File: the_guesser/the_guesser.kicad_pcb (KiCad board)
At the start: 4 copper layers, 24 x 72 mm, 59 parts, among them J1 USB_B_Mini, J2 Conn_Coaxial, J3 RFShield_TwoPieces, U2 ESP32-S3, U3 W25Q128JVS, U5 CC1101RGPR, U6 CC1190RGVR, U7 B39921B3728U410, X1 STDCRG2-27M, X2 ECS-3953M-400-AU-TR

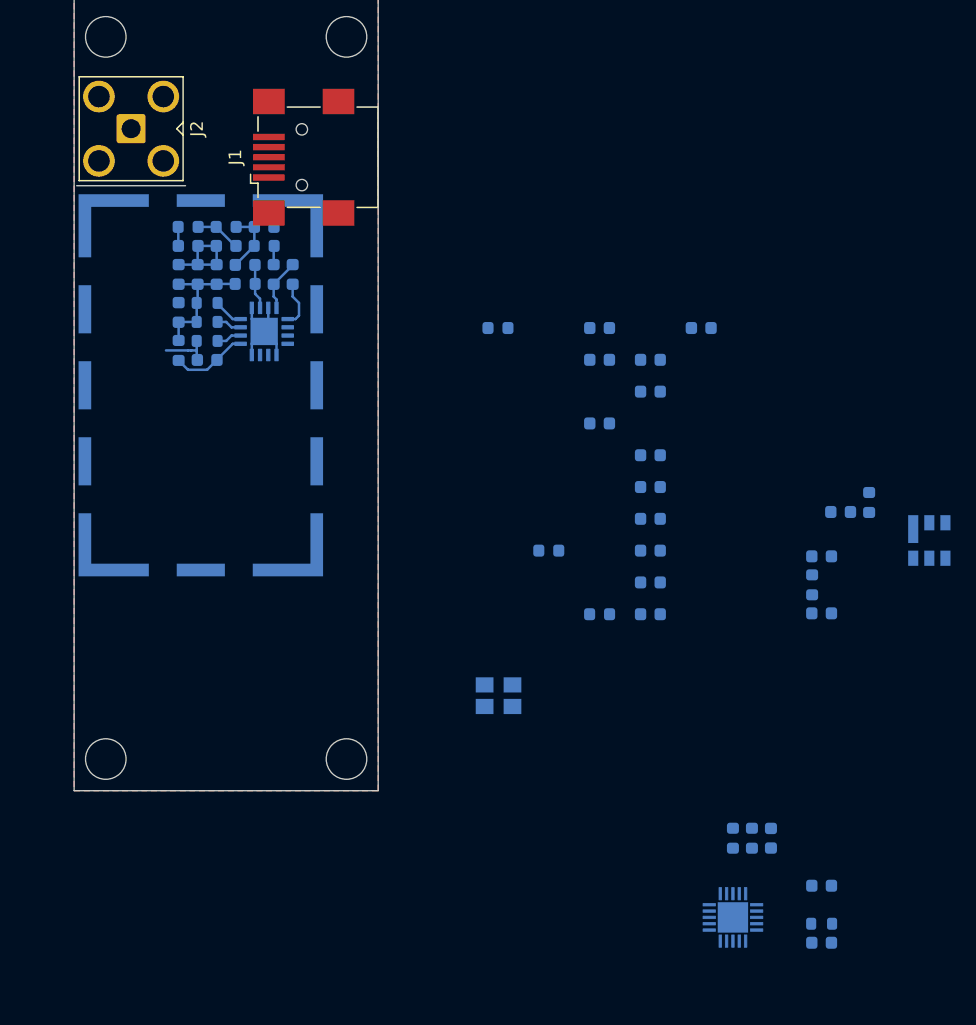
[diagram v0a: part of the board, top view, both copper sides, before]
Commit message: Routed Guesser RF components
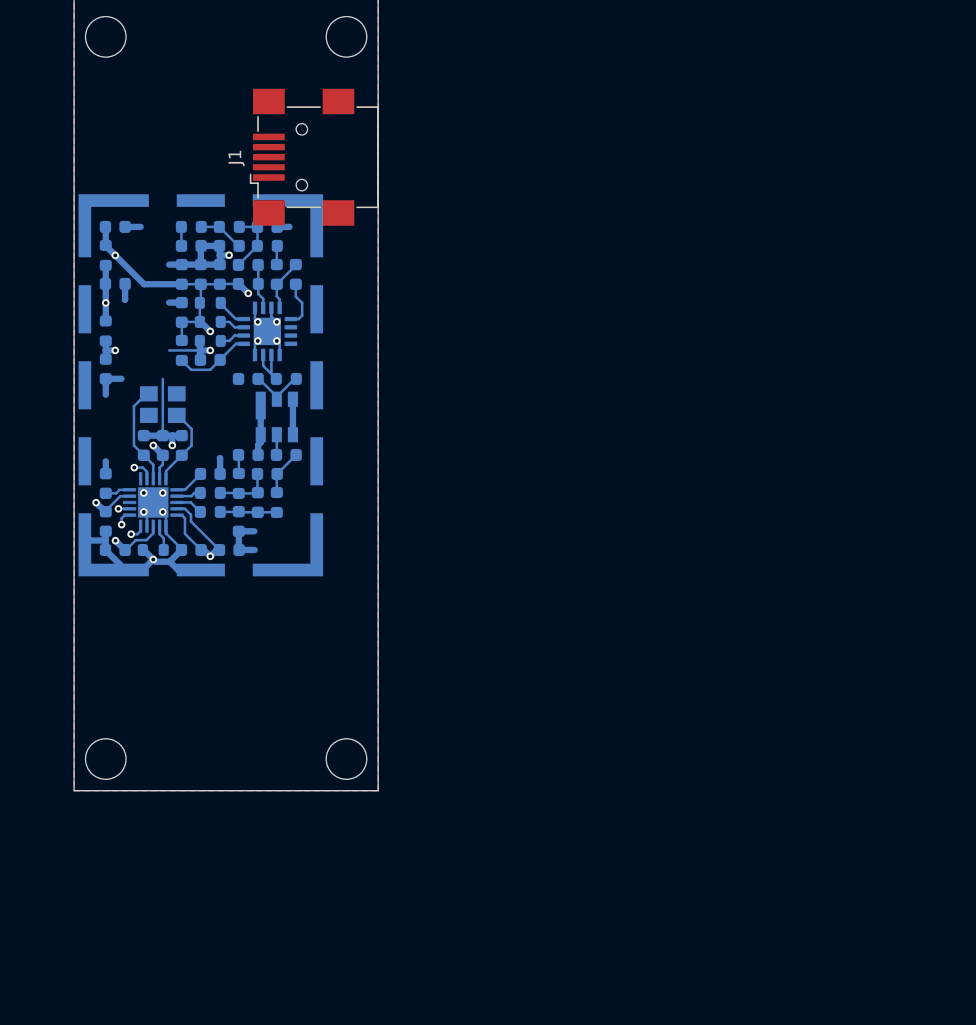
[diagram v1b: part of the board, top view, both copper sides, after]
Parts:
- removed J2: Conn_Coaxial, Connector_Coaxial:SMA_Amphenol_901-143_Horizontal
- J3: value RFShield_TwoPieces -> BMI-S-209-F
- moved C181 63.8 mm to (203.2, 81.0), turned to 0 degrees
- moved C2 61.5 mm to (203.2, 55.5)
- moved C3 61.5 mm to (203.2, 60.0)
- moved L2 61.5 mm to (202.5, 57.8)
- moved R171 60.4 mm to (206.2, 81.0), turned to 0 degrees
- moved C151 56.4 mm to (209.2, 81.0), turned to 0 degrees
- moved U5 56.3 mm to (206.2, 77.2), turned to 0 degrees
- moved U7 52.4 mm to (216.0, 70.5)
- moved L131 49.9 mm to (210.8, 78.0), turned to 180 degrees
- moved L121 49.4 mm to (210.8, 76.5), turned to 0 degrees
- moved C141 48.4 mm to (212.2, 81.0), turned to 180 degrees
- moved C125 47.9 mm to (213.8, 67.5)
- moved C1 47.1 mm to (202.5, 66.7), turned to -90 degrees
- moved L25 47.0 mm to (216.8, 67.5), turned to 180 degrees
- moved L1 44.9 mm to (202.5, 63.7), turned to -90 degrees
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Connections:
- net Net-(U5-AVDD_11) renamed VCC_{CC1101}
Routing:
- net VCC_{CC1101}: track 0.00 -> 54.9 mm, vias 0 -> 5
- net GND: track 20.2 -> 62.5 mm, vias 0 -> 12
- net VCC_{CC1190}: track 10.4 -> 36.4 mm, vias 0 -> 3
- net XOSC_Q1: track 0.00 -> 7.74 mm
- net XOSC_Q2: track 0.00 -> 6.29 mm
- net Net-(C121-Pad2): track 0.00 -> 4.38 mm
- net VCC: track 0.00 -> 4.34 mm, vias 0 -> 1
- net Net-(C121-Pad1): track 0.00 -> 4.31 mm
- net Net-(U7-IN): track 0.00 -> 3.96 mm
- net LNA_OUT: track 0.00 -> 3.82 mm
- net Net-(C122-Pad1): track 0.00 -> 3.56 mm
- net RF_N: track 0.00 -> 2.15 mm
- net Net-(U5-RBIAS): track 0.00 -> 2.01 mm
- net Net-(U5-DCOUPL): track 0.00 -> 1.99 mm
- net RF_P: track 0.00 -> 1.95 mm
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
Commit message: Started Guesser sensor selection
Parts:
- removed X2: ECS-3953M-400-AU-TR, Crystal:Crystal_SMD_5032-4Pin_5.0x3.2mm
- added BT1: Battery_Cell, locals_but_working_PLEASE:CONN2_1775469-2_TEC, F.Cu at (212.0, 100.0)
- added C4: 10u, Capacitor_SMD:C_0603_1608Metric, B.Cu at (207.8, 98.8)
- added D1: MB6S, Package_TO_SOT_SMD:TO-269AA, B.Cu at (212.0, 95.5)
- added J4: Screw_Terminal_01x06, TerminalBlock_Phoenix:TerminalBlock_Phoenix_MPT-0,5-6-2.54_1x06_P2.54mm_Horizontal, F.Cu at (215.6, 42.4)
- added J5: Screw_Terminal_01x06, TerminalBlock_Phoenix:TerminalBlock_Phoenix_MPT-0,5-6-2.54_1x06_P2.54mm_Horizontal, F.Cu at (208.4, 29.6)
- added L3: 0.47u, Inductor_SMD:L_0603_1608Metric, B.Cu at (207.8, 91.5)
- added R2: 5.36k, Resistor_SMD:R_0603_1608Metric, B.Cu at (208.5, 96.5)
- added R3: 1.2k, Resistor_SMD:R_0603_1608Metric, B.Cu at (207.0, 96.5)
- added U10: TPS61033DRLR, Package_TO_SOT_SMD:SOT-583-8, B.Cu at (207.8, 93.7)
- added U8: MS5607-02BA, Package_LGA:LGA-8_3x5mm_P1.25mm, F.Cu at (228.9, 87.1)
- moved U3 85.2 mm to (235.5, 77.0)
- moved U2 78.5 mm to (212.0, 75.0), turned to -45 degrees
- moved J1 37.9 mm to (206.0, 86.0), turned to -90 degrees
- moved C1 8.98 mm to (204.5, 58.0)
- moved X1 8.98 mm to (209.0, 60.8)
- moved C101 8.98 mm to (210.5, 64.0)
- moved C111 8.98 mm to (212.8, 66.2)
- moved C121 8.98 mm to (216.5, 68.5)
- moved C122 8.98 mm to (217.2, 66.2)
- moved C123 8.98 mm to (218.8, 64.8)
- moved C124 8.98 mm to (215.8, 64.8)
- moved C125 8.98 mm to (215.8, 58.8)
- moved C131 8.98 mm to (215.0, 70.0)
- moved C132 8.98 mm to (212.8, 57.2)
- moved C141 8.98 mm to (214.2, 72.2)
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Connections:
- net V_{BAT} renamed V_{USB}
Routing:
- net VCC: track 4.34 -> 13.1 mm, vias 1 -> 3
- net /BT-: track 0.00 -> 6.19 mm, vias 0 -> 1
- net /BT+: track 0.00 -> 6.19 mm, vias 0 -> 1
- net V_{B}: track 0.00 -> 5.02 mm
- net Net-(U10-FB): track 0.00 -> 3.04 mm
- net Net-(U10-SW): track 0.00 -> 2.76 mm
- net GND: track 62.5 -> 63.5 mm

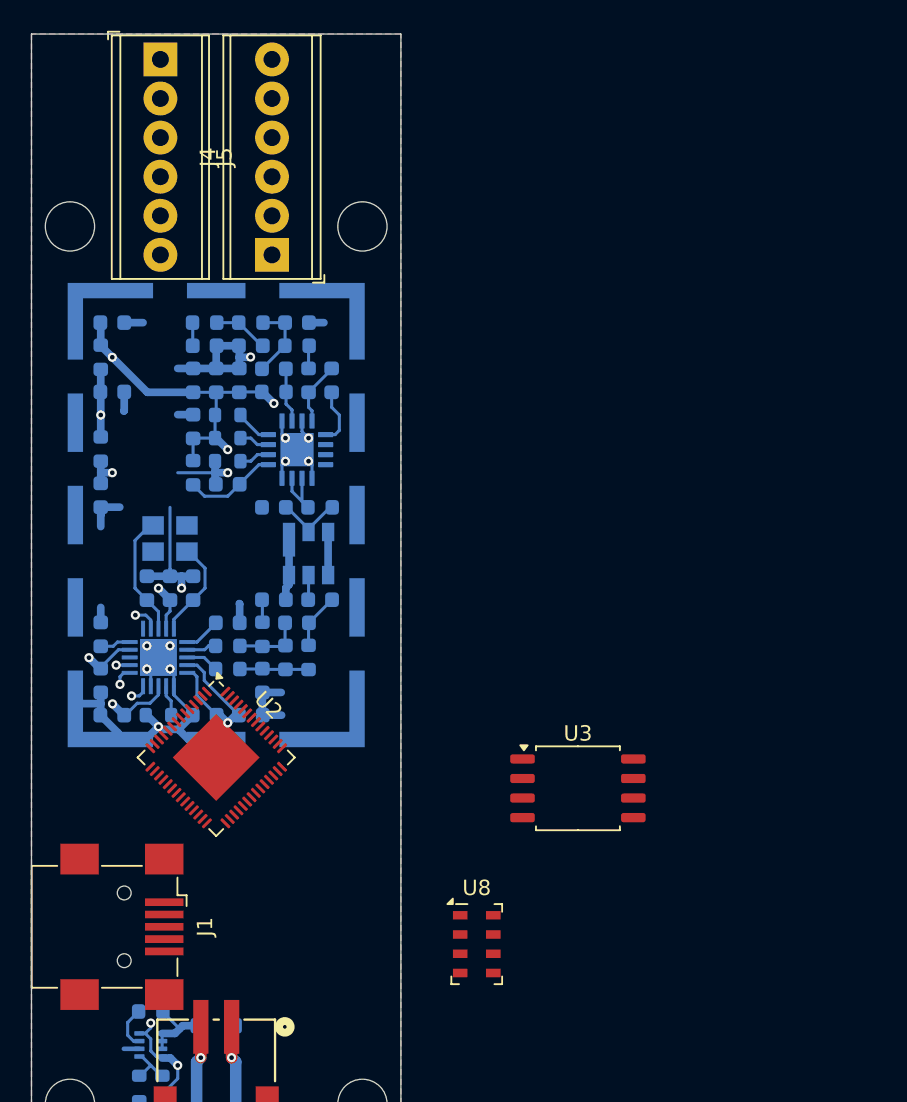
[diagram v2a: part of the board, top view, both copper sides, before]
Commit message: Started Guesser I/O and continued sensor selection
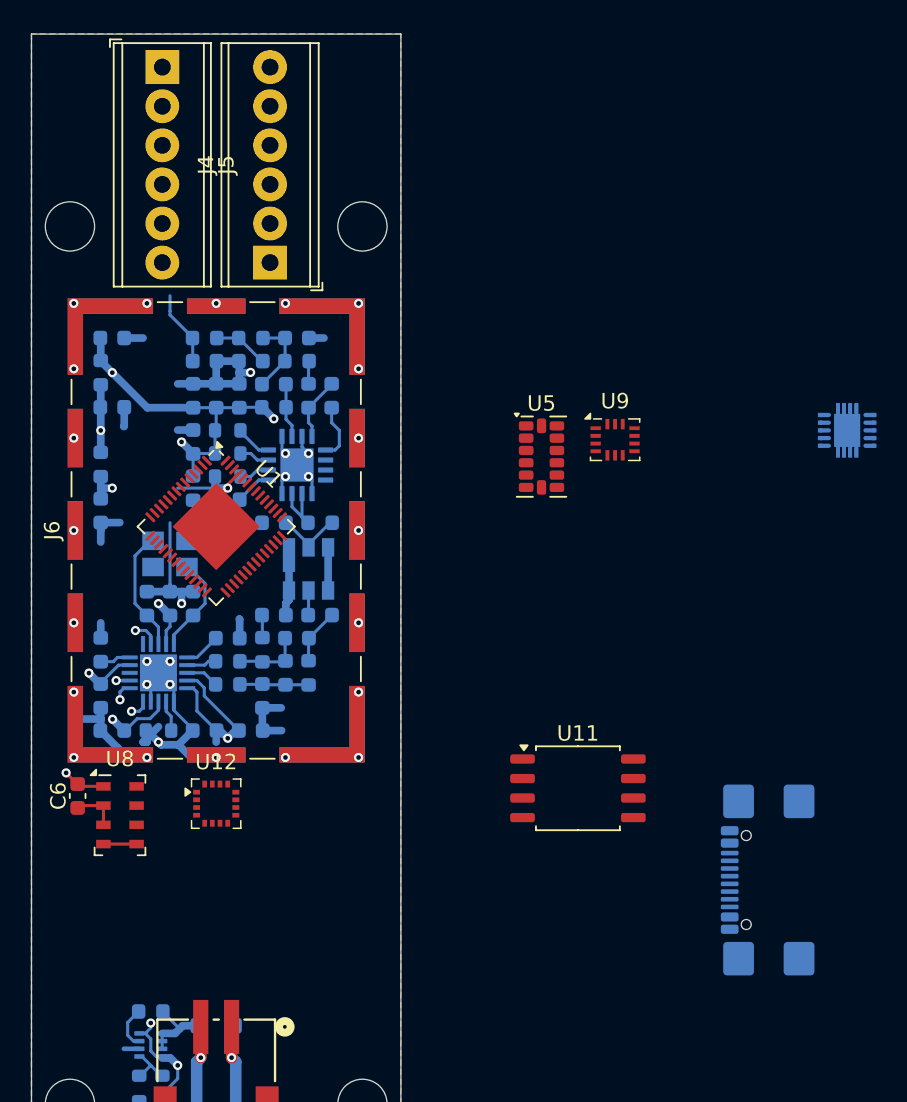
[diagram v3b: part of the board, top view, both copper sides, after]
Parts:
- removed J1: USB_B_Mini, Connector_USB:USB_Mini-B_Wuerth_65100516121_Horizontal
- added C6: 0.1u, Capacitor_SMD:C_0603_1608Metric, F.Cu at (203.0, 77.5)
- added J6: BMI-S-209-F, RF_Shielding:Laird_Technologies_BMI-S-209-F_29.36x18.50mm, F.Cu at (212.0, 60.2)
- added J7: USB_C_Receptacle_USB2.0_16P, Connector_USB:USB_C_Receptacle_GCT_USB4110, B.Cu at (249.0, 83.0)
- added U12: MMC5883MA, Package_LGA:LGA-16_3x3mm_P0.5mm, F.Cu at (212.0, 78.0)
- added U5: ADXL343, Package_LGA:LGA-14_3x5mm_P0.8mm_LayoutBorder1x6y, F.Cu at (233.1, 55.5)
- added U7: TPD4S014, Package_SON:Texas_S-PWSON-N10, B.Cu at (253.0, 53.8)
- added U9: BMI160, Package_LGA:Bosch_LGA-14_3x2.5mm_P0.5mm, F.Cu at (237.9, 54.4)
- moved U8 24.6 mm to (205.8, 78.8)
- moved U1 15.0 mm to (212.0, 60.0)
- moved C1 1.00 mm to (204.5, 59.0)
- moved C101 1.00 mm to (210.5, 65.0)
- moved C111 1.00 mm to (212.8, 67.2)
- moved C121 1.00 mm to (216.5, 69.5)
- moved C122 1.00 mm to (217.2, 67.2)
- moved C123 1.00 mm to (218.8, 65.8)
- moved C124 1.00 mm to (215.8, 65.8)
- moved C125 1.00 mm to (215.8, 59.8)
- moved C131 1.00 mm to (215.0, 71.0)
- moved C132 1.00 mm to (212.8, 58.2)
- moved C141 1.00 mm to (214.2, 73.2)
- moved C151 1.00 mm to (211.2, 73.2)
- moved C161 1.00 mm to (210.5, 54.5)
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- renumbered U2 to U1, U3 to U11, U5 to U2, U6 to U3, U7 to U4
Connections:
- net MISO renamed SDO2
- net MOSI renamed SDI2
- net Net-(U8-CSB-Pad4) renamed ~{CS}_{BARO}
- net SCLK renamed SCLK2
- U1 pad 17: ~{CS} -> unconnected-(U1-GPIO12-Pad17)
- U1 pad 18: ~{MMCS} -> unconnected-(U1-GPIO13-Pad18)
- U1 pad 2: +3V3 -> Net-(U1-VDD3P3-Pad2)
- U1 pad 20: +3V3 -> unconnected-(U1-VDD3P3_RTC-Pad20)
- U1 pad 29: +3V3 -> unconnected-(U1-VDD_SPI-Pad29)
- U1 pad 3: +3V3 -> Net-(U1-VDD3P3-Pad2)
- U1 pad 46: +3V3 -> unconnected-(U1-VDD3P3_CPU-Pad46)
- U1 pad 53: GND -> unconnected-(U1-XTAL_N-Pad53)
- U1 pad 54: f_{CC1200} -> unconnected-(U1-XTAL_P-Pad54)
- U1 pad 55: +3V3 -> Net-(U1-VDDA-Pad55)
- U1 pad 56: +3V3 -> Net-(U1-VDDA-Pad55)
- U11 pad 1: ~{MMCS} -> ~{CS}_{FLASH}
- U11 pad 8: +3V3 -> VCC
- U2 pad 7: ~{CS} -> ~{CS}_{RF}
- U8 pad 1: unconnected-(U8-VDD-Pad1) -> VCC
- U8 pad 2: unconnected-(U8-PS-Pad2) -> GND
- U8 pad 3: unconnected-(U8-GND-Pad3) -> GND
- U8 pad 6: unconnected-(U8-SDO-Pad6) -> SDO1
- U8 pad 7: unconnected-(U8-SDI/SDA-Pad7) -> SDI1
- U8 pad 8: unconnected-(U8-SCLK-Pad8) -> SCLK1
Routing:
- net GND: track 63.5 -> 71.4 mm, vias 12 -> 32
- net Net-(C28-Pad2): track 1.49 -> 4.84 mm
- net VCC: track 13.1 -> 15.9 mm, vias 3 -> 4
- net ~{CS}_{BARO}: track 0.00 -> 2.15 mm
- net VCC_{CC1190}: track 36.4 -> 34.3 mm
- net ~{CS}_{RF}: track 0.00 -> 1.69 mm, vias 0 -> 1
- net ~{CS}: track 1.69 -> 0.00 mm, vias 1 -> 0
